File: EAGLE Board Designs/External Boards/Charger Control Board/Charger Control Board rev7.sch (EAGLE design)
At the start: 108 parts, among them K1 RELAY_DPDT, K2 RELAY_DPDT, K3 RELAY_DPDT, K4 RELAY_SOLIDSTATE_NO_, U1 VOLTAGE_REGULATOR_SOT-223_5V, U2 MCP2562FD, U3 LOGICGATE_BUFFER, U4 MCP2562FD, U7 ADM823

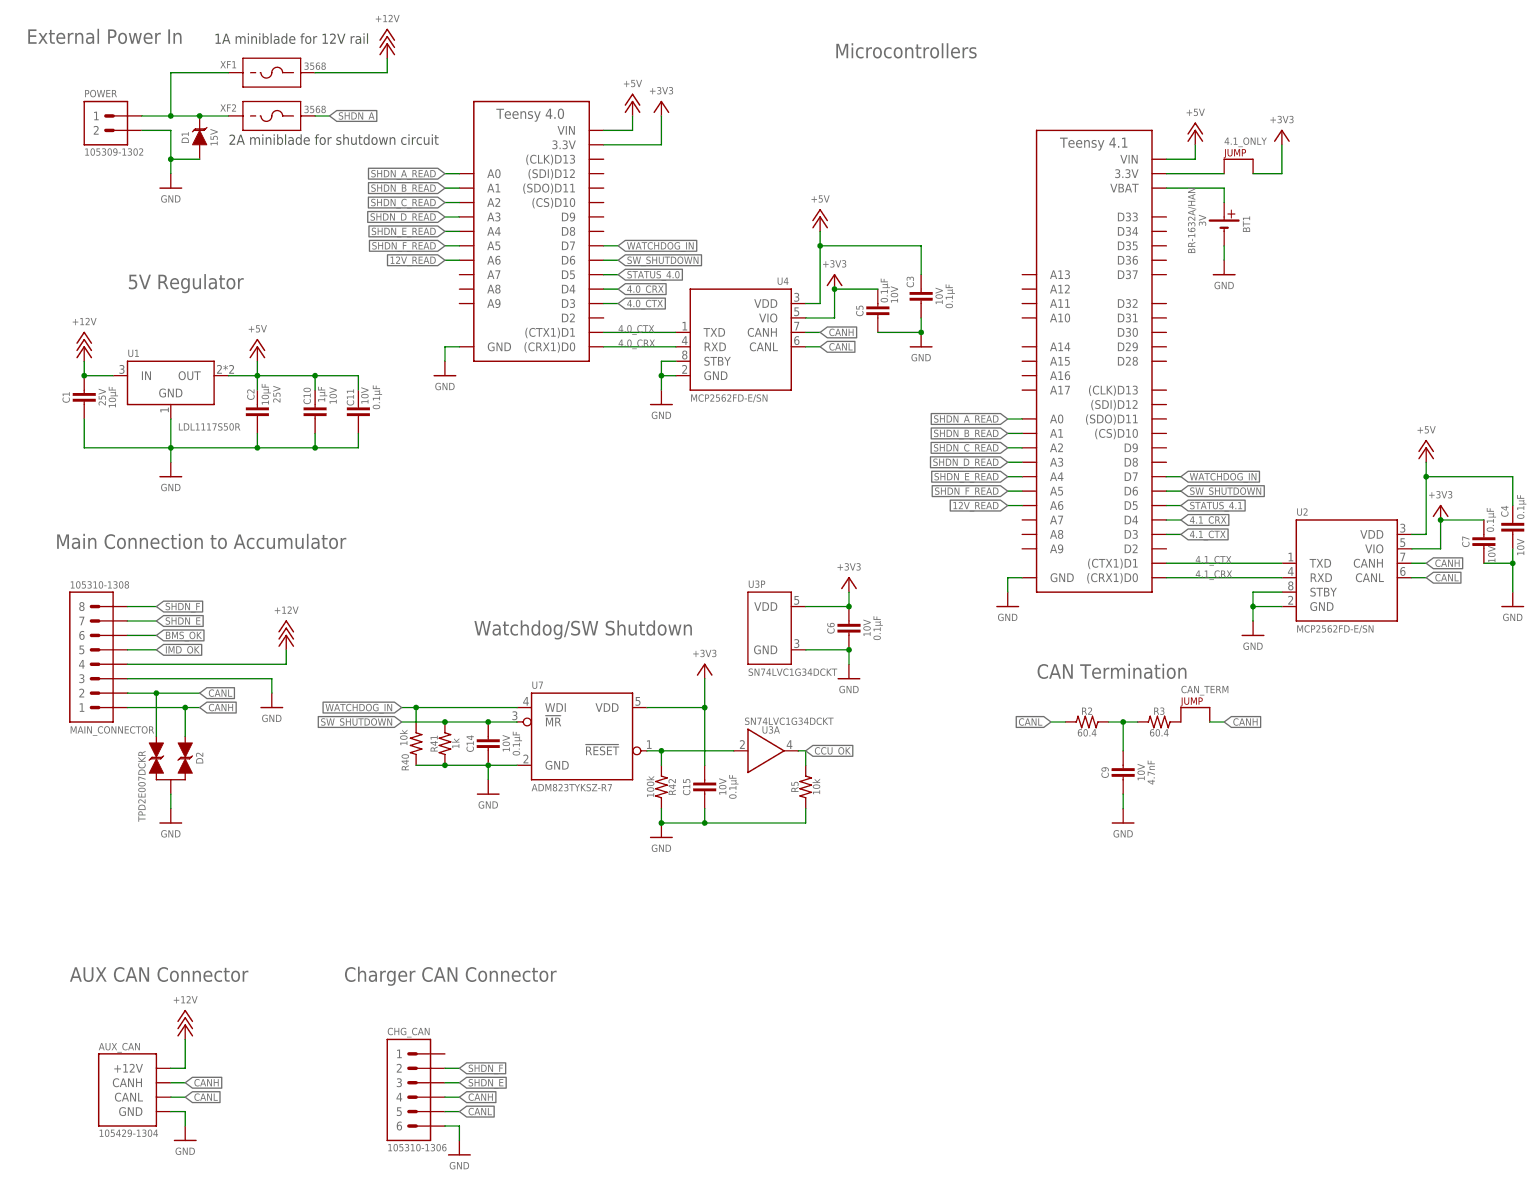
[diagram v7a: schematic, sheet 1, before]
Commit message: Updates following board review
- Renumbered
- Resistor divider values changed
- Added extra tvs protection
- Swapped watchdog
- Fixed LED colors
- Added RPC control relay, jumpers for triggering off of SHDN E and F
- Adjusted silkscreen
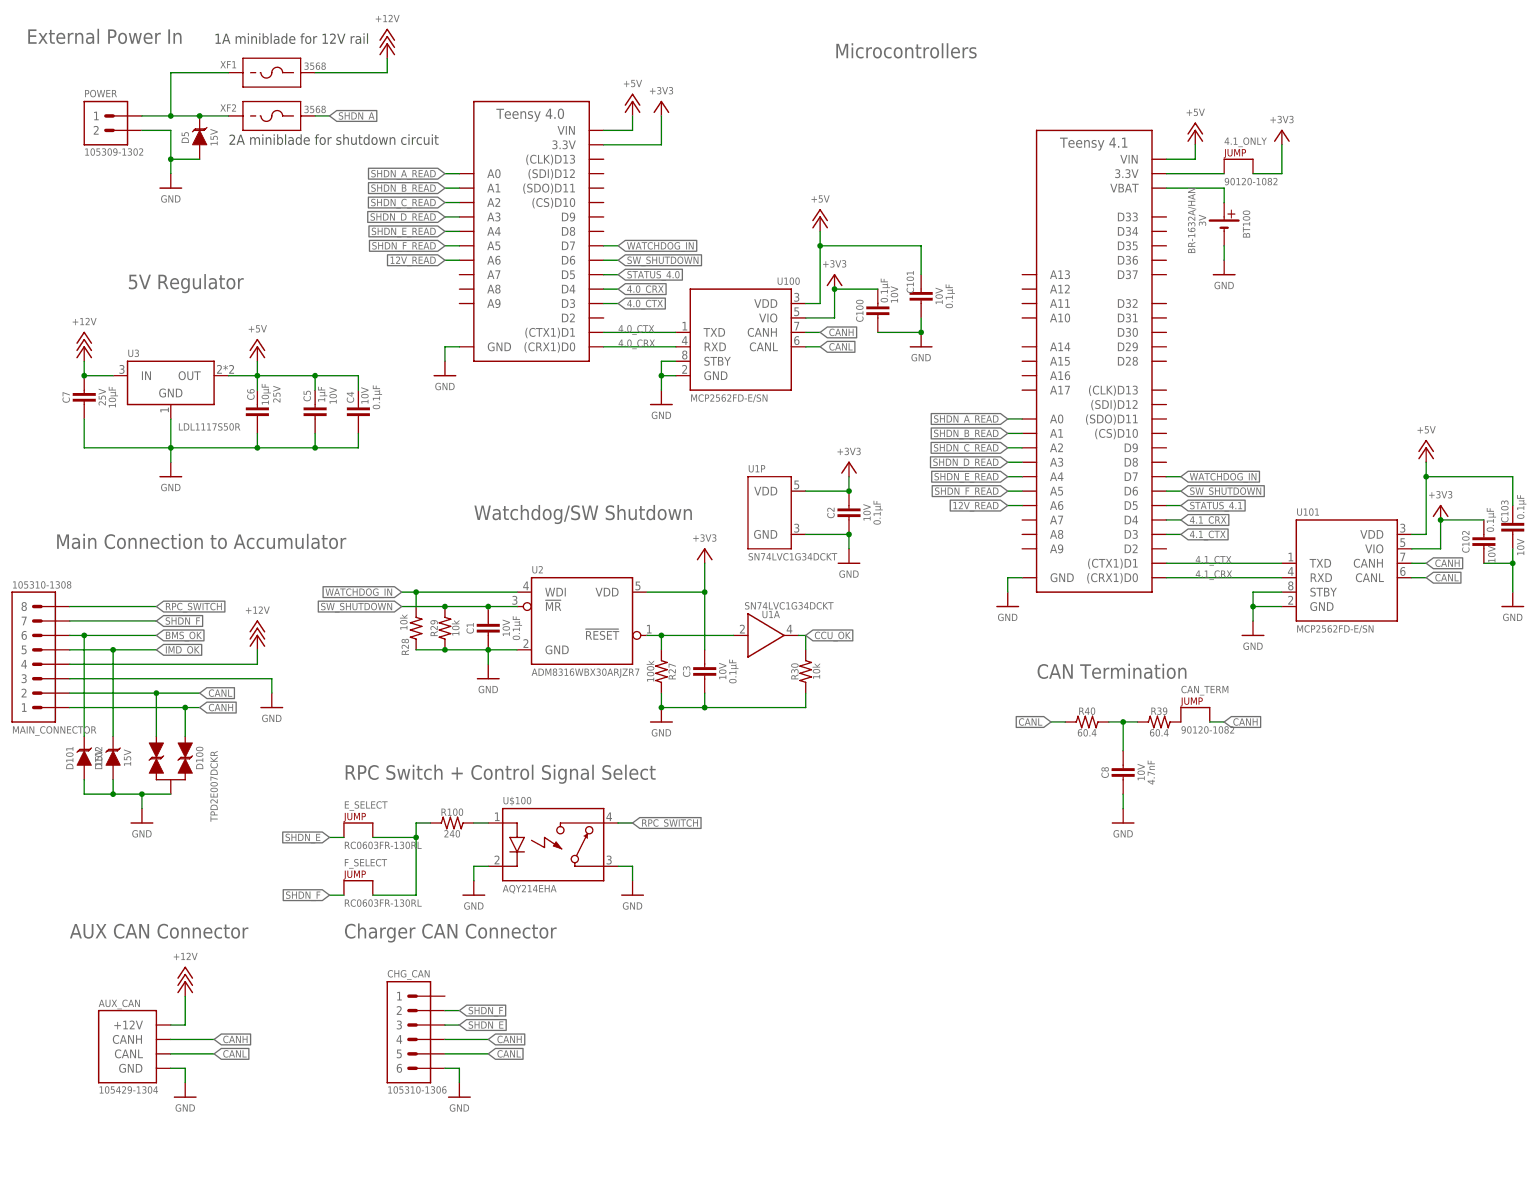
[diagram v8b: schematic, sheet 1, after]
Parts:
- removed C10: CAPACITOR_0603_10V_1UF, HyTechDevices:CAPACITOR_0603_10V_1UF
- removed C11, C14, C15: CAPACITOR_0603_10V_0.1UF, HyTechDevices:CAPACITOR_0603_10V_0.1UF
- removed D6, SHUTDOWN_F, SOFTWARE: LED_0603_RED, HyTechDevices:LED_0603_RED
- removed K4: RELAY_SOLIDSTATE_NO_, HyTechDevicesTempTSB:RELAY_SOLIDSTATE_NO_
- removed R41: RESISTOR_0603_1K, HyTechDevices:RESISTOR_0603_1K
- removed R42: RESISTOR_0603_100K, HyTechDevices:RESISTOR_0603_100K
- removed U7: ADM823, HyTechDevices:ADM823
- added C100, C101, C102, C103: CAPACITOR_0603_10V_0.1UF, HyTechDevices:CAPACITOR_0603_10V_0.1UF
- added CCU_OK: LED_0603_GREEN, HyTechDevices:LED_0603_GREEN
- added D100: TVS_BIDIRECTIONAL_DUAL, HyTechDevices:TVS_BIDIRECTIONAL_DUAL
- added D101, D102: TVS_15V, HyTechDevices:TVS_15V
- added E_SELECT, F_SELECT: JUMPER_0603_, HyTechDevices_Jumper:JUMPER_0603_
- added R100: RESISTOR_0603_240, HyTechDevices_Jumper:RESISTOR_0603_240
- added R38: RESISTOR_0603_1K, HyTechDevices:RESISTOR_0603_1K
- added R39: RESISTOR_0603_60.4, HyTechDevices:RESISTOR_0603_60.4
- added SHDN_F: LED_0603_ORANGE, HyTechDevices:LED_0603_ORANGE
- added U$100, U$4: RELAY_SOLIDSTATE_NO, HyTechDevices:RELAY_SOLIDSTATE_NO
- added U101: MCP2562FD, HyTechDevices:MCP2562FD
- 4.1_ONLY, CAN_TERM: value JUMPER__ -> JUMPER__1X02; device HyTechDevices:JUMPER__ -> HyTechDevices_Jumper:JUMPER__1X02
- A1: value TEENSY_4.0 -> TEENSY_4.1; device HyTechDevices:TEENSY_4.0 -> HyTechDevices:TEENSY_4.1
- A2: value TEENSY_4.1 -> TEENSY_4.0; device HyTechDevices:TEENSY_4.1 -> HyTechDevices:TEENSY_4.0
- C1, C2: value CAPACITOR_0603_25V_10UF -> CAPACITOR_0603_10V_0.1UF; device HyTechDevices:CAPACITOR_0603_25V_10UF -> HyTechDevices:CAPACITOR_0603_10V_0.1UF
- C5: value CAPACITOR_0603_10V_0.1UF -> CAPACITOR_0603_10V_1UF; device HyTechDevices:CAPACITOR_0603_10V_0.1UF -> HyTechDevices:CAPACITOR_0603_10V_1UF
- C6, C7: value CAPACITOR_0603_10V_0.1UF -> CAPACITOR_0603_25V_10UF; device HyTechDevices:CAPACITOR_0603_10V_0.1UF -> HyTechDevices:CAPACITOR_0603_25V_10UF
- D1: value TVS_15V -> SCHOTTKY_SOD323_30V; device HyTechDevices:TVS_15V -> HyTechDevices:SCHOTTKY_SOD323_30V
- D2: value TVS_BIDIRECTIONAL_DUAL -> SCHOTTKY_SOD323_30V; device HyTechDevices:TVS_BIDIRECTIONAL_DUAL -> HyTechDevices:SCHOTTKY_SOD323_30V
- D3: value SCHOTTKY_SOD323_30V -> LED_0603_RED; device HyTechDevices:SCHOTTKY_SOD323_30V -> HyTechDevices:LED_0603_RED
- D5: value SCHOTTKY_SOD323_30V -> TVS_15V; device HyTechDevices:SCHOTTKY_SOD323_30V -> HyTechDevices:TVS_15V
- R1: value RESISTOR_0603_240 -> RESISTOR_0603_1K; device HyTechDevices:RESISTOR_0603_240 -> HyTechDevices:RESISTOR_0603_1K
- R10: value RESISTOR_0603_22 -> RESISTOR_0603_12K; device HyTechDevices:RESISTOR_0603_22 -> HyTechDevices:RESISTOR_0603_12K
- R11, R15, R16: value RESISTOR_0603_1K -> RESISTOR_0603_12K; device HyTechDevices:RESISTOR_0603_1K -> HyTechDevices:RESISTOR_0603_12K
- R12, R13, R14: value RESISTOR_0603_10K -> RESISTOR_0603_12K; device HyTechDevices:RESISTOR_0603_10K -> HyTechDevices:RESISTOR_0603_12K
- R17, R18, R19: value RESISTOR_0603_1K -> RESISTOR_0603_33K; device HyTechDevices:RESISTOR_0603_1K -> HyTechDevices:RESISTOR_0603_33K
- R2, R3: value RESISTOR_0603_60.4 -> RESISTOR_0603_1K; device HyTechDevices:RESISTOR_0603_60.4 -> HyTechDevices:RESISTOR_0603_1K
- R20, R22: value RESISTOR_0603_43K -> RESISTOR_0603_33K; device HyTechDevices:RESISTOR_0603_43K -> HyTechDevices:RESISTOR_0603_33K
- R21, R23: value RESISTOR_0603_12K -> RESISTOR_0603_33K; device HyTechDevices:RESISTOR_0603_12K -> HyTechDevices:RESISTOR_0603_33K
- R24, R28: value RESISTOR_0603_43K -> RESISTOR_0603_10K; device HyTechDevices:RESISTOR_0603_43K -> HyTechDevices:RESISTOR_0603_10K
- R25: value RESISTOR_0603_12K -> RESISTOR_0603_22; device HyTechDevices:RESISTOR_0603_12K -> HyTechDevices:RESISTOR_0603_22
- R26, R35, R6: value RESISTOR_0603_43K -> RESISTOR_0603_1K; device HyTechDevices:RESISTOR_0603_43K -> HyTechDevices:RESISTOR_0603_1K
- R27: value RESISTOR_0603_12K -> RESISTOR_0603_100K; device HyTechDevices:RESISTOR_0603_12K -> HyTechDevices:RESISTOR_0603_100K
- R29, R36: value RESISTOR_0603_12K -> RESISTOR_0603_10K; device HyTechDevices:RESISTOR_0603_12K -> HyTechDevices:RESISTOR_0603_10K
- R30, R33: value RESISTOR_0603_1K -> RESISTOR_0603_10K; device HyTechDevices:RESISTOR_0603_1K -> HyTechDevices:RESISTOR_0603_10K
- R31: value RESISTOR_0603_1K -> RESISTOR_0603_240; device HyTechDevices:RESISTOR_0603_1K -> HyTechDevices:RESISTOR_0603_240
- R34, R37: value RESISTOR_0603_1K -> RESISTOR_0603_22; device HyTechDevices:RESISTOR_0603_1K -> HyTechDevices:RESISTOR_0603_22
- R40: value RESISTOR_0603_10K -> RESISTOR_0603_60.4; device HyTechDevices:RESISTOR_0603_10K -> HyTechDevices:RESISTOR_0603_60.4
- R5: value RESISTOR_0603_10K -> RESISTOR_0603_1K; device HyTechDevices:RESISTOR_0603_10K -> HyTechDevices:RESISTOR_0603_1K
- R7: value RESISTOR_0603_12K -> RESISTOR_0603_1K; device HyTechDevices:RESISTOR_0603_12K -> HyTechDevices:RESISTOR_0603_1K
- R8, R9: value RESISTOR_0603_22 -> RESISTOR_0603_1K; device HyTechDevices:RESISTOR_0603_22 -> HyTechDevices:RESISTOR_0603_1K
- U1: value VOLTAGE_REGULATOR_SOT-223_5V -> LOGICGATE_BUFFER; device HyTechDevices:VOLTAGE_REGULATOR_SOT-223_5V -> HyTechDevices:LOGICGATE_BUFFER
- U2: value MCP2562FD -> ADM8316WBX30; device HyTechDevices:MCP2562FD -> HyTechDevices:ADM8316WBX30
- U3: value LOGICGATE_BUFFER -> VOLTAGE_REGULATOR_SOT-223_5V; device HyTechDevices:LOGICGATE_BUFFER -> HyTechDevices:VOLTAGE_REGULATOR_SOT-223_5V
- renumbered BT1 to BT100, C9 to C8, D10 to D103, D7 to D105, D9 to D104, STATUS_4.0 to STATUS_4.2, U4 to U100
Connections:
- new net N$10: R100.2, U$100.CONTROL+
- new net N$5: E_SELECT.2, F_SELECT.2, R100.1
- new net RPC_SWITCH: MAIN_CONNECTOR.8, U$100.CONTACT2
- net +12V: now also C7.1, R17.1, TP13.P$1, U$4.CONTACT2, U3.IN; no longer C1.1, K4.CONTACT2, R28.1, TP2.P$1, U1.IN
- net +3V3: now also 4.1_ONLY.2, A2.3.3V, C100.2, C102.2, C2.2, C3.2, U101.VIO, U1P.VDD, U2.VDD; no longer 4.1_ONLY.P$2, A1.3.3V, C15.2, C5.2, C6.2, C7.2, U2.VIO, U3P.VDD, U7.VDD
- net +5V: now also C101.2, C103.2, C5.1, C6.1, TP12.P$1, U101.VDD, U3.OUT; no longer C10.1, C11.2, C2.1, C3.2, TP1.P$1, U1.OUT, U2.VDD
- net 12V_READ: now also R10.1, R17.2; no longer R28.2, R29.1
- net 4.0_CRX: now also A2.(CRX1)D0, A2.D4; no longer A1.(CRX1)D0, A1.D4
- net 4.0_CTX: now also A2.(CTX1)D1, A2.D3; no longer A1.(CTX1)D1, A1.D3
- net 4.1_CRX: now also A1.(CRX1)D0, A1.D4, U101.RXD; no longer A2.(CRX1)D0, A2.D4, U2.RXD
- net 4.1_CTX: now also A1.(CTX1)D1, A1.D3, U101.TXD; no longer A2.(CTX1)D1, A2.D3, U2.TXD
- net BMS_OK: now also D101.C, R33.2, R34.2, TP6.P$1; no longer R13.2, R8.2, TP10.P$1
- net CANH: now also CAN_TERM.2, D100.C1, U101.CANH; no longer CAN_TERM.P$2, D2.C1, U2.CANH
- net CANL: now also D100.C2, R40.1, U101.CANL; no longer D2.C2, R2.1, U2.CANL
- net CCU_OK: now also CCU_OK.A, R30.2, R31.2, U1A.OUT; no longer R1.2, R5.2, SOFTWARE.A, U3A.OUT
- net GND: now also C1.1, C100.1, C101.1, C102.1, C103.1, C2.1, C5.2, C6.2, C7.2, D100.A, D101.A, D102.A, D3.C, D5.A, R1.2, R10.2, R11.2, R12.2, R13.2, R14.2, R15.2, R16.2, R2.2, R24.1, R26.2, R28.2, R29.1, R30.1, R33.1, R36.1, R8.2, R9.2, TP1.P$1, U$100.CONTACT1, U$100.CONTROL-, U$4.CONTROL-, U101.GND, U101.STBY, U1P.GND, U3.GND; no longer C1.2, C10.2, C11.1, C14.1, C15.1, C2.2, C5.1, C6.1, C7.1, D1.A, D2.A, D6.C, K4.CONTROL-, R12.1, R13.1, R14.1, R21.2, R23.2, R25.2, R29.2, R30.2, R31.2, R33.2, R34.2, R36.2, R37.2, R4.2, R40.2, R41.1, R42.2, R5.1, TP12.P$1, U1.GND, U2.STBY, U3P.GND, U7.GND
- net IMD_OK: now also D102.C, R24.2, R25.2, TP7.P$1; no longer R10.2, R14.2, TP9.P$1
- net LATCH_BUTTON: now also D1.C, D2.C, R35.2; no longer D3.C, D5.C, R15.2
- net N$1: now also D5.C; no longer D1.C
- net N$11: now also D1.A; no longer D3.A
- net N$12: now also R25.1; no longer R10.1
- net N$13: now also R34.1; no longer R8.1
- net N$14: now also D2.A; no longer D4.A
- net N$15: now also R37.1; no longer R9.1
- net N$16: now also R36.2, R37.2, R38.1, U$4.CONTACT1; no longer K4.CONTACT1, R11.1, R12.2, R9.2
- net N$17: now also R35.1; no longer R15.1
- net N$18: now also R5.2; no longer R17.2
- net N$19: now also R6.2; no longer R16.2
- net N$2: now also R27.1, U1A.IN, U2.!RESET!; no longer R42.1, U3A.IN, U7.!RESET!
- net N$20: now also D4.A; no longer D5.A
- net N$21: now also D3.A, R38.2; no longer D6.A, R11.2
- net N$22: now also R4.2; no longer R18.2
- net N$23: now also R3.2; no longer R19.2
- net N$29: now also R7.1; no longer R30.1
- net N$3: now also R8.1, SHDN_F.C; no longer R33.1, SHUTDOWN_F.C
- net N$30: now also R2.1; no longer R31.1
- net N$31: now also CCU_OK.C, R9.1; no longer R32.1, SOFTWARE.C
- net N$33: now also R26.1; no longer R34.1
- net N$35: now also R32.1; no longer R37.1
- net N$36: now also 4.1_ONLY.1, A1.3.3V; no longer 4.1_ONLY.P$1, A2.3.3V
- net N$39: now also R1.1; no longer R4.1
- net N$4: now also CAN_TERM.1, R39.2; no longer CAN_TERM.P$1, R3.2
- net N$6: now also R31.1, U$4.CONTROL+; no longer K4.CONTROL+, R1.1
- net N$8: now also A1.VBAT; no longer A2.VBAT
- net N$9: now also R39.1, R40.2; no longer R2.2, R3.1
- net SHDN_A: now also R23.1, TP10.P$1; no longer R20.1, TP3.P$1
- net SHDN_A_READ: now also R16.1, R23.2; no longer R20.2, R21.1
- net SHDN_B: now also R3.1, TP2.P$1; no longer R19.1, TP4.P$1
- net SHDN_B_READ: now also R15.1; no longer R23.1
- net SHDN_C: now also R21.1, R4.1, TP3.P$1; no longer R18.1, R24.1, TP5.P$1
- net SHDN_C_READ: now also R14.1, R21.2; no longer R24.2, R25.1
- net SHDN_D: now also R20.1, R5.1, TP4.P$1; no longer R17.1, R26.1, TP6.P$1
- net SHDN_D_READ: now also R13.1, R20.2; no longer R26.2, R27.1
- net SHDN_E: now also E_SELECT.1, R19.1, R6.1, TP5.P$1; no longer MAIN_CONNECTOR.7, R16.1, R35.1, TP7.P$1
- net SHDN_E_READ: now also R12.1, R19.2; no longer R35.2, R36.1
- net SHDN_F: now also F_SELECT.1, MAIN_CONNECTOR.7, R18.1, SHDN_F.A, TP9.P$1; no longer MAIN_CONNECTOR.8, R6.1, SHUTDOWN_F.A, TP13.P$1
- net SHDN_F_READ: now also R11.1, R18.2; no longer R6.2, R7.1
- net STATUS_4.0: now also A2.D5; no longer A1.D5
- net STATUS_4.1: now also A1.D5; no longer A2.D5
- net SW_SHUTDOWN: now also C1.2, R29.2, U2.!MR!; no longer C14.2, R41.2, U7.!MR!
- net WATCHDOG_IN: now also R28.1, U2.WDI; no longer R40.1, U7.WDI
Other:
- note added: "RPC Switch + Control Signal Select"
- moved on the sheet: AUX_CAN, C1, C2, C3, C4, C5, C6, C7, CHG_CAN, D4, MAIN_CONNECTOR, R1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
